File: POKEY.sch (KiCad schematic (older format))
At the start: 66 parts, among them J108 pin, J109 pin, J110 pin, J111 pin, J201 Diagnostic, J211 Diag, U22 POKEY, U24 CD4051B, U25 CD4051B

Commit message: Tracking
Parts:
- C69, C70: footprint Atari:C_Axial_L5.1mm_D2.5mm_P12.50mm_Horizontal -> Capacitor_SMD:C_1206_3216Metric_Pad1.42x1.75mm_HandSolder
- R137, R138, R139, R140, R141, R142, R143, R144, R145, R146, R147, R148, R149, R150, R151, R152, R153, R89, R90: footprint Atari:R_Axial_DIN0207_L3.6mm_D2.2mm_P10.16mm_Horizontal -> Resistor_SMD:R_1206_3216Metric_Pad1.42x1.75mm_HandSolder
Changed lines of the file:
@@
 F 0 "R146" V 9375 1650 50  0000 C CNN
 F 1 "220" V 9325 1825 50  0000 C CNN
-F 2 "Atari:R_Axial_DIN0207_L3.6mm_D2.2mm_P10.16mm_Horizontal" V 9305 1650 50  0001 C CNN
+F 2 "Resistor_SMD:R_1206_3216Metric_Pad1.42x1.75mm_HandSolder" V 9305 1650 50  0001 C CNN
 F 3 "~" H 9375 1650 50  0001 C CNN
 	1    9375 1650
@@
 F 0 "R147" V 9375 1750 50  0000 C CNN
 F 1 "220" V 9325 1925 50  0000 C CNN
-F 2 "Atari:R_Axial_DIN0207_L3.6mm_D2.2mm_P10.16mm_Horizontal" V 9305 1750 50  0001 C CNN
+F 2 "Resistor_SMD:R_1206_3216Metric_Pad1.42x1.75mm_HandSolder" V 9305 1750 50  0001 C CNN
 F 3 "~" H 9375 1750 50  0001 C CNN
 	1    9375 1750
@@
 F 0 "R148" V 9375 1850 50  0000 C CNN
 F 1 "220" V 9325 2025 50  0000 C CNN
-F 2 "Atari:R_Axial_DIN0207_L3.6mm_D2.2mm_P10.16mm_Horizontal" V 9305 1850 50  0001 C CNN
+F 2 "Resistor_SMD:R_1206_3216Metric_Pad1.42x1.75mm_HandSolder" V 9305 1850 50  0001 C CNN
 F 3 "~" H 9375 1850 50  0001 C CNN
 	1    9375 1850
@@
 F 0 "R149" V 9375 1950 50  0000 C CNN
 F 1 "220" V 9325 2125 50  0000 C CNN
-F 2 "Atari:R_Axial_DIN0207_L3.6mm_D2.2mm_P10.16mm_Horizontal" V 9305 1950 50  0001 C CNN
+F 2 "Resistor_SMD:R_1206_3216Metric_Pad1.42x1.75mm_HandSolder" V 9305 1950 50  0001 C CNN
 F 3 "~" H 9375 1950 50  0001 C CNN
 	1    9375 1950
@@
 F 0 "R150" V 9375 2050 50  0000 C CNN
 F 1 "220" V 9325 2225 50  0000 C CNN
-F 2 "Atari:R_Axial_DIN0207_L3.6mm_D2.2mm_P10.16mm_Horizontal" V 9305 2050 50  0001 C CNN
+F 2 "Resistor_SMD:R_1206_3216Metric_Pad1.42x1.75mm_HandSolder" V 9305 2050 50  0001 C CNN
 F 3 "~" H 9375 2050 50  0001 C CNN
 	1    9375 2050
@@
 F 0 "R151" V 9375 2150 50  0000 C CNN
 F 1 "220" V 9325 2325 50  0000 C CNN
-F 2 "Atari:R_Axial_DIN0207_L3.6mm_D2.2mm_P10.16mm_Horizontal" V 9305 2150 50  0001 C CNN
+F 2 "Resistor_SMD:R_1206_3216Metric_Pad1.42x1.75mm_HandSolder" V 9305 2150 50  0001 C CNN
 F 3 "~" H 9375 2150 50  0001 C CNN
 	1    9375 2150
@@
 F 0 "R152" V 9375 2250 50  0000 C CNN
 F 1 "220" V 9325 2425 50  0000 C CNN
-F 2 "Atari:R_Axial_DIN0207_L3.6mm_D2.2mm_P10.16mm_Horizontal" V 9305 2250 50  0001 C CNN
+F 2 "Resistor_SMD:R_1206_3216Metric_Pad1.42x1.75mm_HandSolder" V 9305 2250 50  0001 C CNN
 F 3 "~" H 9375 2250 50  0001 C CNN
 	1    9375 2250
@@
 F 0 "R153" V 9375 2350 50  0000 C CNN
 F 1 "220" V 9325 2525 50  0000 C CNN
-F 2 "Atari:R_Axial_DIN0207_L3.6mm_D2.2mm_P10.16mm_Horizontal" V 9305 2350 50  0001 C CNN
+F 2 "Resistor_SMD:R_1206_3216Metric_Pad1.42x1.75mm_HandSolder" V 9305 2350 50  0001 C CNN
 F 3 "~" H 9375 2350 50  0001 C CNN
 	1    9375 2350
@@
 F 0 "C69" H 9400 1150 50  0000 L CNN
 F 1 "100nF" H 9400 1000 50  0000 L CNN
-F 2 "Atari:C_Axial_L5.1mm_D2.5mm_P12.50mm_Horizontal" H 9413 925 50  0001 C CNN
+F 2 "Capacitor_SMD:C_1206_3216Metric_Pad1.42x1.75mm_HandSolder" H 9413 925 50  0001 C CNN
 F 3 "~" H 9375 1075 50  0001 C CNN
 	1    9375 1075
@@
 F 0 "R89" V 7500 1475 50  0000 C CNN
 F 1 "47k" V 7425 1300 50  0000 C CNN
-F 2 "Atari:R_Axial_DIN0207_L3.6mm_D2.2mm_P10.16mm_Horizontal" V 7430 1475 50  0001 C CNN
+F 2 "Resistor_SMD:R_1206_3216Metric_Pad1.42x1.75mm_HandSolder" V 7430 1475 50  0001 C CNN
 F 3 "~" H 7500 1475 50  0001 C CNN
 	1    7500 1475
@@
 F 0 "R145" V 9375 3650 50  0000 C CNN
 F 1 "220" V 9325 3825 50  0000 C CNN
-F 2 "Atari:R_Axial_DIN0207_L3.6mm_D2.2mm_P10.16mm_Horizontal" V 9305 3650 50  0001 C CNN
+F 2 "Resistor_SMD:R_1206_3216Metric_Pad1.42x1.75mm_HandSolder" V 9305 3650 50  0001 C CNN
 F 3 "~" H 9375 3650 50  0001 C CNN
 	1    9375 3650
@@
 F 0 "R144" V 9375 3750 50  0000 C CNN
 F 1 "220" V 9325 3925 50  0000 C CNN
-F 2 "Atari:R_Axial_DIN0207_L3.6mm_D2.2mm_P10.16mm_Horizontal" V 9305 3750 50  0001 C CNN
+F 2 "Resistor_SMD:R_1206_3216Metric_Pad1.42x1.75mm_HandSolder" V 9305 3750 50  0001 C CNN
 F 3 "~" H 9375 3750 50  0001 C CNN
 	1    9375 3750
@@
 F 0 "R143" V 9375 3850 50  0000 C CNN
 F 1 "220" V 9325 4025 50  0000 C CNN
-F 2 "Atari:R_Axial_DIN0207_L3.6mm_D2.2mm_P10.16mm_Horizontal" V 9305 3850 50  0001 C CNN
+F 2 "Resistor_SMD:R_1206_3216Metric_Pad1.42x1.75mm_HandSolder" V 9305 3850 50  0001 C CNN
 F 3 "~" H 9375 3850 50  0001 C CNN
 	1    9375 3850
@@
 F 0 "R142" V 9375 3950 50  0000 C CNN
 F 1 "220" V 9325 4125 50  0000 C CNN
-F 2 "Atari:R_Axial_DIN0207_L3.6mm_D2.2mm_P10.16mm_Horizontal" V 9305 3950 50  0001 C CNN
+F 2 "Resistor_SMD:R_1206_3216Metric_Pad1.42x1.75mm_HandSolder" V 9305 3950 50  0001 C CNN
 F 3 "~" H 9375 3950 50  0001 C CNN
 	1    9375 3950
@@
 F 0 "R141" V 9375 4050 50  0000 C CNN
 F 1 "220" V 9325 4225 50  0000 C CNN
-F 2 "Atari:R_Axial_DIN0207_L3.6mm_D2.2mm_P10.16mm_Horizontal" V 9305 4050 50  0001 C CNN
+F 2 "Resistor_SMD:R_1206_3216Metric_Pad1.42x1.75mm_HandSolder" V 9305 4050 50  0001 C CNN
 F 3 "~" H 9375 4050 50  0001 C CNN
 	1    9375 4050
@@
 F 0 "R140" V 9375 4150 50  0000 C CNN
 F 1 "220" V 9325 4325 50  0000 C CNN
-F 2 "Atari:R_Axial_DIN0207_L3.6mm_D2.2mm_P10.16mm_Horizontal" V 9305 4150 50  0001 C CNN
+F 2 "Resistor_SMD:R_1206_3216Metric_Pad1.42x1.75mm_HandSolder" V 9305 4150 50  0001 C CNN
 F 3 "~" H 9375 4150 50  0001 C CNN
 	1    9375 4150
@@
 F 0 "R139" V 9375 4250 50  0000 C CNN
 F 1 "220" V 9325 4425 50  0000 C CNN
-F 2 "Atari:R_Axial_DIN0207_L3.6mm_D2.2mm_P10.16mm_Horizontal" V 9305 4250 50  0001 C CNN
+F 2 "Resistor_SMD:R_1206_3216Metric_Pad1.42x1.75mm_HandSolder" V 9305 4250 50  0001 C CNN
 F 3 "~" H 9375 4250 50  0001 C CNN
 	1    9375 4250
@@
 F 0 "R138" V 9375 4350 50  0000 C CNN
 F 1 "220" V 9325 4525 50  0000 C CNN
-F 2 "Atari:R_Axial_DIN0207_L3.6mm_D2.2mm_P10.16mm_Horizontal" V 9305 4350 50  0001 C CNN
+F 2 "Resistor_SMD:R_1206_3216Metric_Pad1.42x1.75mm_HandSolder" V 9305 4350 50  0001 C CNN
 F 3 "~" H 9375 4350 50  0001 C CNN
 	1    9375 4350
@@
 F 0 "R137" V 4575 3400 50  0000 C CNN
 F 1 "270" V 4525 3575 50  0000 C CNN
-F 2 "Atari:R_Axial_DIN0207_L3.6mm_D2.2mm_P10.16mm_Horizontal" V 4505 3400 50  0001 C CNN
+F 2 "Resistor_SMD:R_1206_3216Metric_Pad1.42x1.75mm_HandSolder" V 4505 3400 50  0001 C CNN
 F 3 "~" H 4575 3400 50  0001 C CNN
 	1    4575 3400
@@
 F 0 "R90" V 7550 3750 50  0000 C CNN
 F 1 "100" V 7500 3925 50  0000 C CNN
-F 2 "Atari:R_Axial_DIN0207_L3.6mm_D2.2mm_P10.16mm_Horizontal" V 7480 3750 50  0001 C CNN
+F 2 "Resistor_SMD:R_1206_3216Metric_Pad1.42x1.75mm_HandSolder" V 7480 3750 50  0001 C CNN
 F 3 "~" H 7550 3750 50  0001 C CNN
 	1    7550 3750
@@
 F 0 "C70" H 9400 3075 50  0000 L CNN
 F 1 "100nF" H 9400 2925 50  0000 L CNN
-F 2 "Atari:C_Axial_L5.1mm_D2.5mm_P12.50mm_Horizontal" H 9413 2850 50  0001 C CNN
+F 2 "Capacitor_SMD:C_1206_3216Metric_Pad1.42x1.75mm_HandSolder" H 9413 2850 50  0001 C CNN
 F 3 "~" H 9375 3000 50  0001 C CNN
 	1    9375 3000

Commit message: Change THT on SMD
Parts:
- C98: footprint Capacitor_THT:CP_Axial_L11.0mm_D6.0mm_P18.00mm_Horizontal -> Capacitor_THT:CP_Radial_D5.0mm_P2.00mm
- D5: footprint Diode_THT:D_DO-35_SOD27_P12.70mm_Horizontal -> Diode_SMD:D_1206_3216Metric_Pad1.42x1.75mm_HandSolder
- R96: footprint Atari:R_Axial_DIN0207_L3.6mm_D2.2mm_P10.16mm_Horizontal -> Resistor_SMD:R_1206_3216Metric_Pad1.42x1.75mm_HandSolder
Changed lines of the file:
@@
 F 0 "D5" V 4000 3175 50  0000 L CNN
 F 1 "1N4148" H 3775 3050 50  0000 L CNN
-F 2 "Diode_THT:D_DO-35_SOD27_P12.70mm_Horizontal" H 3875 2975 50  0001 C CNN
+F 2 "Diode_SMD:D_1206_3216Metric_Pad1.42x1.75mm_HandSolder" H 3875 2975 50  0001 C CNN
 F 3 "https://assets.nexperia.com/documents/data-sheet/1N4148_1N4448.pdf" H 3875 3150 50  0001 C CNN
 	1    3875 3150
@@
 F 0 "R96" V 4075 3150 50  0000 C CNN
 F 1 "47k" V 4025 3325 50  0000 C CNN
-F 2 "Atari:R_Axial_DIN0207_L3.6mm_D2.2mm_P10.16mm_Horizontal" V 4005 3150 50  0001 C CNN
+F 2 "Resistor_SMD:R_1206_3216Metric_Pad1.42x1.75mm_HandSolder" V 4005 3150 50  0001 C CNN
 F 3 "~" H 4075 3150 50  0001 C CNN
 	1    4075 3150
@@
 F 0 "C98" H 4168 4696 50  0000 L CNN
 F 1 "10uF" H 4168 4605 50  0000 L CNN
-F 2 "Capacitor_THT:CP_Axial_L11.0mm_D6.0mm_P18.00mm_Horizontal" H 4088 4500 50  0001 C CNN
+F 2 "Capacitor_THT:CP_Radial_D5.0mm_P2.00mm" H 4088 4500 50  0001 C CNN
 F 3 "~" H 4050 4650 50  0001 C CNN
 	1    4050 4650

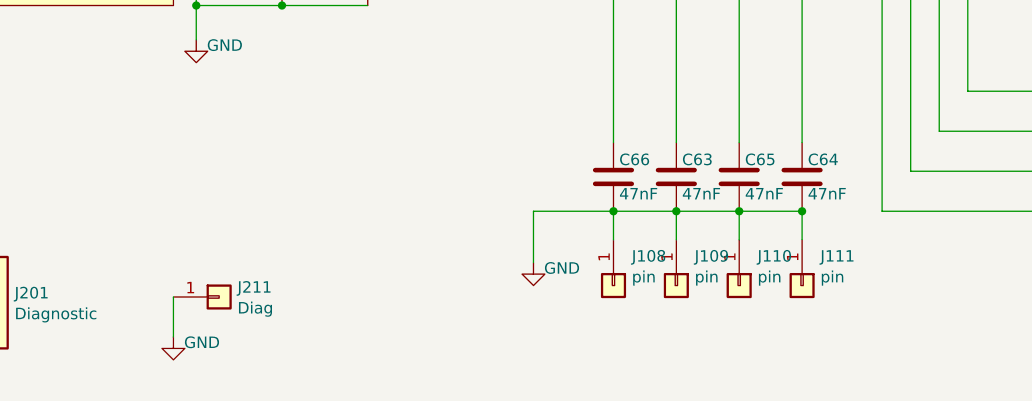
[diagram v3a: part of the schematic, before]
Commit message: OSS and Basic in PLCC
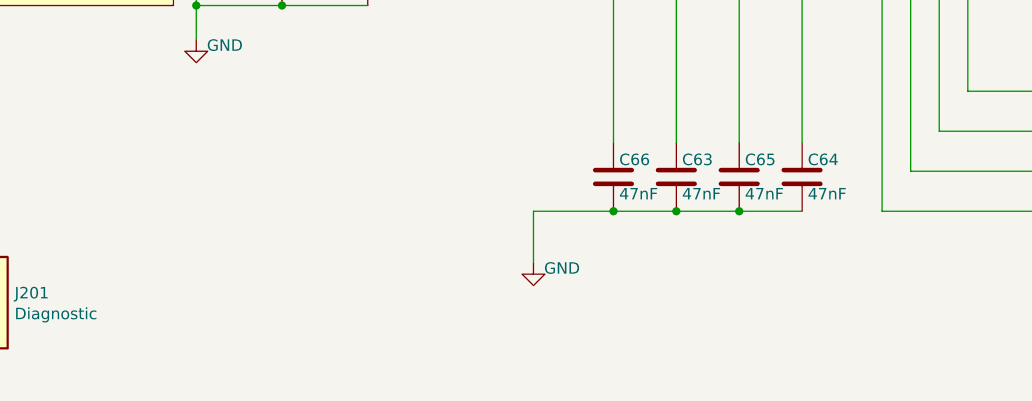
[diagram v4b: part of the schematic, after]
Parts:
- removed J108, J109, J110, J111: pin, Connector_PinHeader_2.00mm:PinHeader_1x01_P2.00mm_Vertical, symbol Connector_Generic:Conn_01x01
- removed J211: Diag, Connector_PinHeader_2.54mm:PinHeader_1x01_P2.54mm_Vertical, symbol Connector_Generic:Conn_01x01
- C62, C63, C64, C65, C66, C71, C72, C73, C74, C75, C76, C77, C78: footprint Atari:C_Axial_L5.1mm_D2.5mm_P12.50mm_Horizontal -> Capacitor_SMD:C_1206_3216Metric_Pad1.42x1.75mm_HandSolder
- L15, L16, L17, L18: footprint Atari:L_Axial_L7.0mm_D3.3mm_P12.50mm_Horizontal_Fastron_MICC -> Inductor_SMD:L_1812_4532Metric_Pad1.30x3.40mm_HandSolder
- R128, R129, R130, R131, R76, R77, R78, R79, R80, R81, R82, R83, R84: footprint Atari:R_Axial_DIN0207_L3.6mm_D2.2mm_P10.16mm_Horizontal -> Resistor_SMD:R_1206_3216Metric_Pad1.42x1.75mm_HandSolder
